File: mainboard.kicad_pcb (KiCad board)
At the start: 2 copper layers, 147 parts, among them IC1 ATXMEGA128A1U-A, J1 USB, K1 X_MIN, K2 X_MAX, K3 Y_MIN, K4 Y_MAX, K5 Z_MIN, K6 Z_MAX, P1 POWER, P10 USART, P11 TH_HB, P12 TH_EX, P13 TH_HO, P14 LCD, P15 STP_Y, P16 STP_E0, P17 STP_X, P18 STP_E1, P19 STP_Z, P2 PDI, P20 EXTR, P21 HIC_0, P22 HEATBED, P23 HIC_1, P24 FAN_0, P25 FAN_1, P26 LOC_0, P27 LOC_1, P3 GPIO_B, P4 BEEPER, P5 OPEN_C_OUT, P6 12V, P7 5V, P8 3.3V, P9 I2C, Q1 IRL1404, Q2 IRL1404, Q3 IRL1404, Q4 IRL1404, U1 NE 4558 D SMD, U10 ULN_2003_A, U2 ULN_2003_A, U3 A4988-BO, U4 A4988-BO, U5 A4988-BO, U6 A4988-BO, U7 A4988-BO, U8 MCP14E10, U9 MCP14E10

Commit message: Added missing interface connector; reworked schematic. Started to layout PCB
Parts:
- added D20: LOC0, LEDs:LED-0603, F.Cu at (157.7, 45.0)
- added D21: LOC1, LEDs:LED-0603, F.Cu at (184.2, 19.5)
- added R31: 4.7k, SMD_Packages:SM0805, F.Cu at (158.4, 42.0)
- added R32: 4.7k, SMD_Packages:SM0805, F.Cu at (162.3, 39.7)
- C1, C3: value 100n -> 470uF; footprint SMD_Packages:SM0603_Capa -> Capacitors_SMD:c_elec_10x10
- C17: value 100uF -> 100n; footprint Capacitors_SMD:c_elec_6.3x7.7 -> SMD_Packages:SM0603_Capa
- C2, C5: value 470uF -> 100n; footprint Capacitors_SMD:c_elec_10x10 -> SMD_Packages:SM0603_Capa
- C22: value 100n -> 100uF; footprint SMD_Packages:SM0603_Capa -> Capacitors_SMD:c_elec_6.3x7.7
- D10: value DIODE -> EXTR; footprint Diodes_SMD:Diode-SMA_Handsoldering -> LEDs:LED-0603
- D11: value DIODE -> HIC0; footprint Diodes_SMD:Diode-SMA_Handsoldering -> LEDs:LED-0603
- D12: value HIC1 -> DIODE; footprint LEDs:LED-0603 -> Diodes_SMD:Diode-MELF_Handsoldering
- D13: value HB -> DIODE; footprint LEDs:LED-0603 -> Diodes_SMD:Diode-MELF_Handsoldering
- D14: value DIODE -> HIC1; footprint Diodes_SMD:Diode-SMA_Handsoldering -> LEDs:LED-0603
- D15: value DIODE -> HB; footprint Diodes_SMD:Diode-SMA_Handsoldering -> LEDs:LED-0603
- D16: value FAN0 -> DIODE; footprint LEDs:LED-0603 -> Diodes_SMD:Diode-MELF_Handsoldering
- D17: value FAN1 -> DIODE; footprint LEDs:LED-0603 -> Diodes_SMD:Diode-MELF_Handsoldering
- D18: value LOC0 -> FAN0
- D19: value LOC1 -> FAN1
- D2: value PWR -> PRW 12V
- D3: value ST-E0 -> PWR 5V
- D4: value ST-Y -> PWR 3V3
- D5: value ST-E1 -> ST-E0
- D6: value ST-X -> ST-Y
- D7: value ST-Z -> ST-E1
- D8: value EXTR -> ST-X
- D9: value HIC0 -> ST-Z
- R10: value 5.6k -> 33k
- R12, R13: value 100k -> 5.6k
- R15, R16: value 15k -> 100k
- R18, R19: value 680 -> 15k
- R23, R24: value 4.7k -> 680
- R3: value 680 -> 4.7k
- R4: value 68 -> 1.5k
- R5: value 68 -> 680
- R6, R7: value 10k -> 68
- R8: value 33k -> 10k
- R9: value 5.6k -> 10k
- U10: footprint SMD_Packages:SO14E -> SMD_Packages:SO16E
- moved P3 333.0 mm to (336.5, -29.0)
- moved P14 311.7 mm to (337.5, 15.0)
- moved C12 311.2 mm to (326.0, 69.5)
- moved J1 305.9 mm to (329.5, 80.0)
- moved U2 287.2 mm to (338.0, 141.0)
- moved P5 286.0 mm to (336.5, 151.0)
- moved D1 270.8 mm to (278.5, 15.5)
- moved R6 264.6 mm to (332.5, 66.5)
- moved RV5 263.0 mm to (328.5, 26.0)
- moved C17 257.1 mm to (342.0, 24.5)
- moved R7 252.6 mm to (339.0, 69.0)
- moved VR2 229.9 mm to (327.0, 66.5)
- moved VR1 226.5 mm to (333.0, 69.0)
- moved R4 205.5 mm to (264.0, 36.5), turned to 90 degrees
- moved C8 191.9 mm to (214.5, 103.0), turned to 180 degrees
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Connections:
- C1 pad 1: GND -> +12V
- C1 pad 2: +3.3V -> GND
- C17 pad 1: +12V -> +5V
- C17 pad 2: Net-(C17-Pad2) -> GND
- C2 pad 1: +12V -> GND
- C2 pad 2: GND -> +3.3V
- C22 pad 1: +5V -> +12V
- C22 pad 2: GND -> Net-(C22-Pad2)
- C3 pad 1: GND -> +3.3V
- C3 pad 2: +3.3V -> GND
- C5 pad 1: +3.3V -> GND
- C5 pad 2: GND -> +3.3V
- C6 pad 1: GND -> +3.3V
- C6 pad 2: +3.3V -> GND
- C7 pad 1: +3.3V -> GND
- C7 pad 2: GND -> +3.3V
- D10 pad 2: +12V -> Net-(D10-Pad2)
- D11 pad 2: +12V -> Net-(D11-Pad2)
- D12 pad 1: Net-(D12-Pad1) -> Net-(D11-Pad2)
- D12 pad 2: Net-(D12-Pad2) -> +12V
- D13 pad 1: Net-(D13-Pad1) -> Net-(D10-Pad2)
- D13 pad 2: Net-(D13-Pad2) -> +12V
- D14 pad 1: Net-(D12-Pad2) -> Net-(D14-Pad1)
- D14 pad 2: +12V -> Net-(D14-Pad2)
- D15 pad 1: Net-(D13-Pad2) -> Net-(D15-Pad1)
- D15 pad 2: +12V -> Net-(D15-Pad2)
- D16 pad 1: Net-(D16-Pad1) -> Net-(D14-Pad2)
- D16 pad 2: Net-(D16-Pad2) -> +12V
- D17 pad 1: Net-(D17-Pad1) -> Net-(D15-Pad2)
- D17 pad 2: Net-(D17-Pad2) -> +12V
- D2 pad 1: +3.3V -> +12V
- D3 pad 1: Net-(D3-Pad1) -> +5V
- D4 pad 1: Net-(D4-Pad1) -> +3.3V
- D8 pad 2: Net-(D11-Pad1) -> Net-(D8-Pad2)
- D9 pad 2: Net-(D10-Pad1) -> Net-(D9-Pad2)
- P20 pad 2: Net-(D11-Pad1) -> Net-(D10-Pad2)
- P21 pad 2: Net-(D10-Pad1) -> Net-(D11-Pad2)
- P22 pad 2: Net-(D13-Pad2) -> Net-(D15-Pad2)
- P23 pad 2: Net-(D12-Pad2) -> Net-(D14-Pad2)
- P24 pad 2: Net-(D16-Pad2) -> Net-(D18-Pad2)
- P25 pad 2: Net-(D17-Pad2) -> Net-(D19-Pad2)
- P26 pad 2: Net-(D18-Pad2) -> Net-(D20-Pad2)
- P27 pad 2: Net-(D19-Pad2) -> Net-(D21-Pad2)
- Q1 pad D: Net-(D11-Pad1) -> Net-(D10-Pad2)
- Q2 pad D: Net-(D10-Pad1) -> Net-(D11-Pad2)
- Q3 pad D: Net-(D12-Pad2) -> Net-(D14-Pad2)
- Q4 pad D: Net-(D13-Pad2) -> Net-(D15-Pad2)
- R10 pad 1: GND -> Net-(R10-Pad1)
- R10 pad 2: Net-(P12-Pad2) -> GND
- R11 pad 2: Net-(P13-Pad2) -> Net-(P11-Pad2)
- R12 pad 1: Net-(P11-Pad2) -> GND
- R12 pad 2: /TH_HB -> Net-(P12-Pad2)
- R13 pad 1: Net-(P12-Pad2) -> GND
- R13 pad 2: /TH_EX -> Net-(P13-Pad2)
- R14 pad 1: Net-(P13-Pad2) -> Net-(P11-Pad2)
- R14 pad 2: /TH_HO -> /TH_HB
- R15 pad 1: +3.3V -> Net-(P12-Pad2)
- R15 pad 2: Net-(P11-Pad2) -> /TH_EX
- R16 pad 1: +3.3V -> Net-(P13-Pad2)
- R16 pad 2: Net-(P12-Pad2) -> /TH_HO
- R17 pad 2: Net-(P13-Pad2) -> Net-(P11-Pad2)
- R18 pad 1: Net-(D3-Pad2) -> +3.3V
- R18 pad 2: GND -> Net-(P12-Pad2)
- R19 pad 1: Net-(D4-Pad2) -> +3.3V
- R19 pad 2: GND -> Net-(P13-Pad2)
- R23 pad 1: +12V -> Net-(D8-Pad2)
- R23 pad 2: Net-(D8-Pad1) -> GND
- R24 pad 1: +12V -> Net-(D9-Pad2)
- R24 pad 2: Net-(D9-Pad1) -> GND
- R25 pad 2: Net-(D12-Pad1) -> Net-(D10-Pad1)
- R26 pad 2: Net-(D13-Pad1) -> Net-(D11-Pad1)
- R27 pad 1: Net-(D16-Pad1) -> +12V
- R27 pad 2: +12V -> Net-(D14-Pad1)
- R28 pad 1: Net-(D17-Pad1) -> +12V
- R28 pad 2: +12V -> Net-(D15-Pad1)
- R4 pad 1: Net-(IC1-Pad31) -> Net-(D3-Pad2)
- R4 pad 2: Net-(J1-Pad2) -> GND
- R5 pad 1: Net-(IC1-Pad32) -> Net-(D4-Pad2)
- R5 pad 2: Net-(J1-Pad3) -> GND
- R6 pad 1: /TWIC-SDA -> Net-(IC1-Pad31)
- R6 pad 2: +3.3V -> Net-(J1-Pad2)
- R7 pad 1: /TWIC-SCL -> Net-(IC1-Pad32)
- R7 pad 2: +3.3V -> Net-(J1-Pad3)
- R8 pad 1: Net-(R8-Pad1) -> /TWIC-SDA
- R8 pad 2: GND -> +3.3V
- R9 pad 1: GND -> /TWIC-SCL
- R9 pad 2: Net-(P11-Pad2) -> +3.3V
- RV1 pad 2: Net-(R8-Pad1) -> Net-(R10-Pad1)
- U1 pad 2: Net-(R8-Pad1) -> Net-(R10-Pad1)
- U10 pad 10: Net-(D19-Pad2) -> Net-(D21-Pad2)
- U10 pad 12: Net-(D18-Pad2) -> Net-(D20-Pad2)
- U10 pad 14: Net-(D17-Pad2) -> Net-(D19-Pad2)
- U3 pad 15: Net-(C17-Pad2) -> Net-(C18-Pad2)
- U5 pad 15: Net-(C19-Pad2) -> Net-(C20-Pad2)
- U6 pad 15: Net-(C20-Pad2) -> Net-(C21-Pad2)
- U7 pad 15: Net-(C21-Pad2) -> Net-(C22-Pad2)

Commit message: Reworked schematic
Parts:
- moved JP1 5.90 mm to (80.0, 39.5)
- moved JP2 5.25 mm to (79.5, 44.5)
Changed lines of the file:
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@@
     (links 367)
     (no_connects 367)
-    (area 0 0 0 0)
+    (area 12.7 -35.71195 351.851001 196.031501)
     (thickness 1.6)
     (drawings 0)
@@
     (pad_to_mask_clearance 0)
     (aux_axis_origin 0 0)
-    (grid_origin 10 10)
+    (grid_origin 78 28)
     (visible_elements FFFFF77F)
     (pcbplotparams
@@
   )
   (module Connect:SIL-2 (layer F.Cu)
-    (at 79.491828 45.382018)
+    (at 80 39.5)
     (descr "Connecteurs 2 pins")
     (tags "CONN DEV")
@@
   )
   (module Connect:SIL-2 (layer F.Cu)
-    (at 79.491828 39.252018)
+    (at 79.5 44.5)
     (descr "Connecteurs 2 pins")
     (tags "CONN DEV")

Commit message: * Changed connectors to PSK type - this prevents plugging the steppers in the wrong way * Changed stepping increment jumpers to DIP-switches - easier setting
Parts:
- removed JP1, JP10, JP11, JP12, JP13, JP14, JP15, JP2, JP3, JP4, JP5, JP6, JP7, JP8, JP9: JUMPER, Connect:SIL-2
- added P28: INTERFACE, Connect:VASCH5x2, F.Cu at (243.0, 92.0)
- added SW1: Y, dip-s:DIPS-DS03, F.Cu at (0.00, 0.00)
- added SW2: E0, dip-s:DIPS-DS03, F.Cu at (0.00, 0.00)
- added SW3: X, dip-s:DIPS-DS03, F.Cu at (0.00, 0.00)
- added SW4: E1, dip-s:DIPS-DS03, F.Cu at (0.00, 0.00)
- added SW5: Z, dip-s:DIPS-DS03, F.Cu at (0.00, 0.00)
- P15, P16, P17, P18, P19: footprint Connect:bornier4 -> 3dp-special:PSS4
- P2, P9: footprint Connect:SIL-4 -> 3dp-special:PSS4
- P24, P25, P26, P27: footprint Connect:bornier2 -> Connect:SIL-2
- P5: value OPEN_C_OUT -> OPEN_COLL_D
- moved P16 176.3 mm to (50.0, 191.5)
- moved P18 123.7 mm to (4.00, 173.5)
- moved P15 109.2 mm to (74.5, 165.5)
- moved P17 102.2 mm to (51.0, 139.0)
- moved P19 78.4 mm to (24.0, 135.0)
- moved D12 9.90 mm to (152.0, 34.5)
- moved D18 9.62 mm to (175.0, 41.9)
- moved D19 9.62 mm to (171.1, 44.2)
- moved R26 9.62 mm to (167.9, 41.2)
- moved R31 9.62 mm to (167.9, 43.5)
- moved R32 9.62 mm to (171.8, 41.2)
- moved C22 7.44 mm to (50.5, 48.5)
- moved D16 2.15 mm to (153.0, 39.0)
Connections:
- net /A0 renamed /OCD_1
- net /A1 renamed /OCD_2
- net /A2 renamed /OCD_3
- net /A3 renamed /OCD_4
- net /A4 renamed /OCD_5
- net /A5 renamed /OCD_6
- net /B0 renamed /GPIOB_0
- net /B1 renamed /GPIOB_1
- net /B2 renamed /GPIOB_2
- net /B3 renamed /GPIOB_3
- net /B4 renamed /GPIOB_4
- net /B5 renamed /GPIOB_5
- net /B6 renamed /GPIOB_6
- net /B7 renamed /GPIOB_7
- net Net-(J1-Pad2) renamed /USB-
- net Net-(J1-Pad3) renamed /USB+
- IC1 pad 1: /INP_INTERF4 -> /INTERF4
- IC1 pad 100: /INP_INTERF3 -> /INTERF3
- IC1 pad 2: /INP_INTERF5 -> /INTERF5
- IC1 pad 98: /INP_INTERF1 -> /INTERF1
- IC1 pad 99: /INP_INTERF2 -> /INTERF2
- U4 pad 15: Net-(U4-Pad15) -> Net-(C19-Pad2)
- U4 pad 16: Net-(U4-Pad16) -> +12V

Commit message: * Added PSK-2 connector to library * Changed Low-Current outputs (FANs etc) to PSK-2 connectors
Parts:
- K1, K2, K3, K4, K5, K6: footprint Connect:PINHEAD1-3 -> 3dp-special:PSS3
- P24, P25, P26, P27: footprint Connect:SIL-2 -> 3dp-special:PSS2
- moved SW1 216.6 mm to (120.5, 180.0)
- moved SW2 208.2 mm to (41.5, 204.0)
- moved P8 200.9 mm to (240.5, 37.0)
- moved SW3 190.7 mm to (101.5, 161.5)
- moved SW4 185.8 mm to (26.0, 184.0)
- moved SW5 167.8 mm to (40.0, 163.0)
- moved P24 150.8 mm to (187.0, 156.0)
- moved P26 145.6 mm to (197.5, 150.5)
- moved P27 143.8 mm to (206.0, 151.5)
- moved D21 140.6 mm to (223.5, 154.5)
- moved U10 140.1 mm to (198.5, 161.0)
- moved P2 129.1 mm to (189.5, 73.0)
- moved D20 127.8 mm to (214.5, 159.5)
- moved R26 127.4 mm to (233.9, 150.2)
- moved R32 127.4 mm to (237.8, 150.2)
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
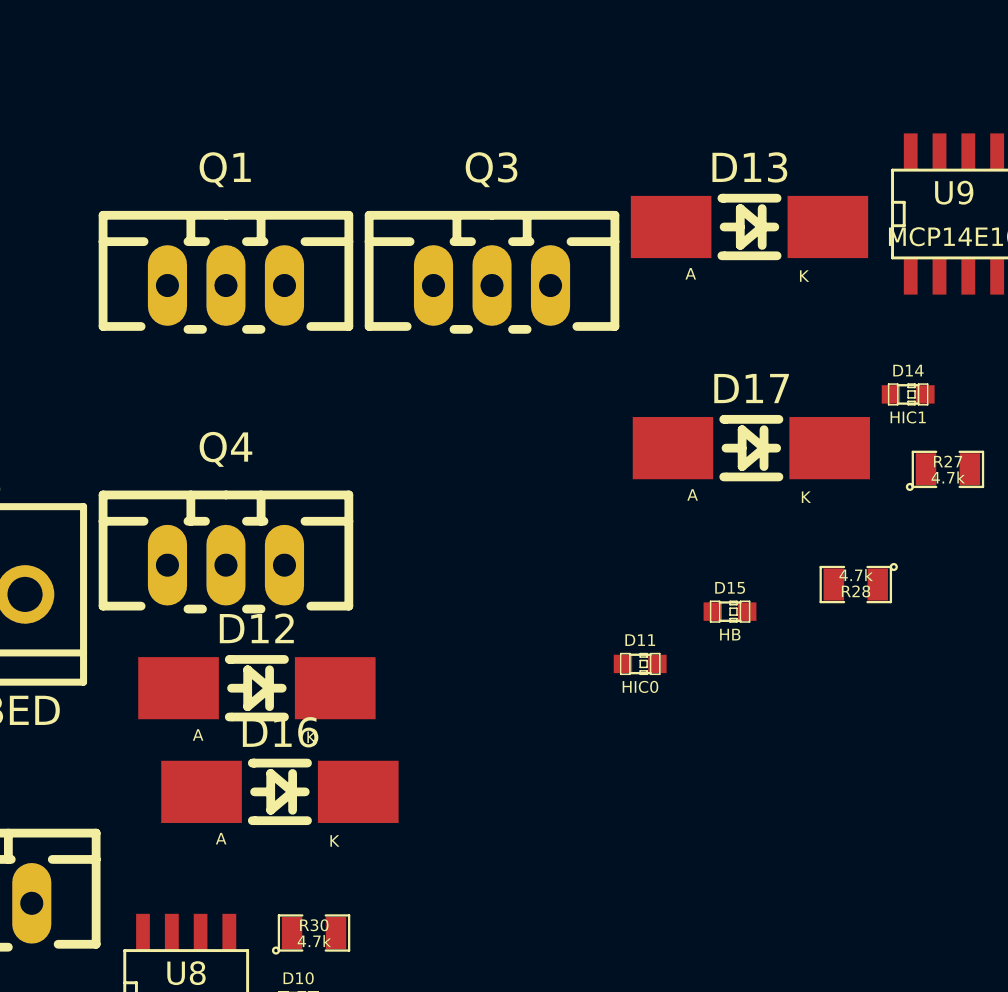
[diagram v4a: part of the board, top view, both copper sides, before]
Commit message: Added footprint for SOD323 diode package and replaced former MELF-package
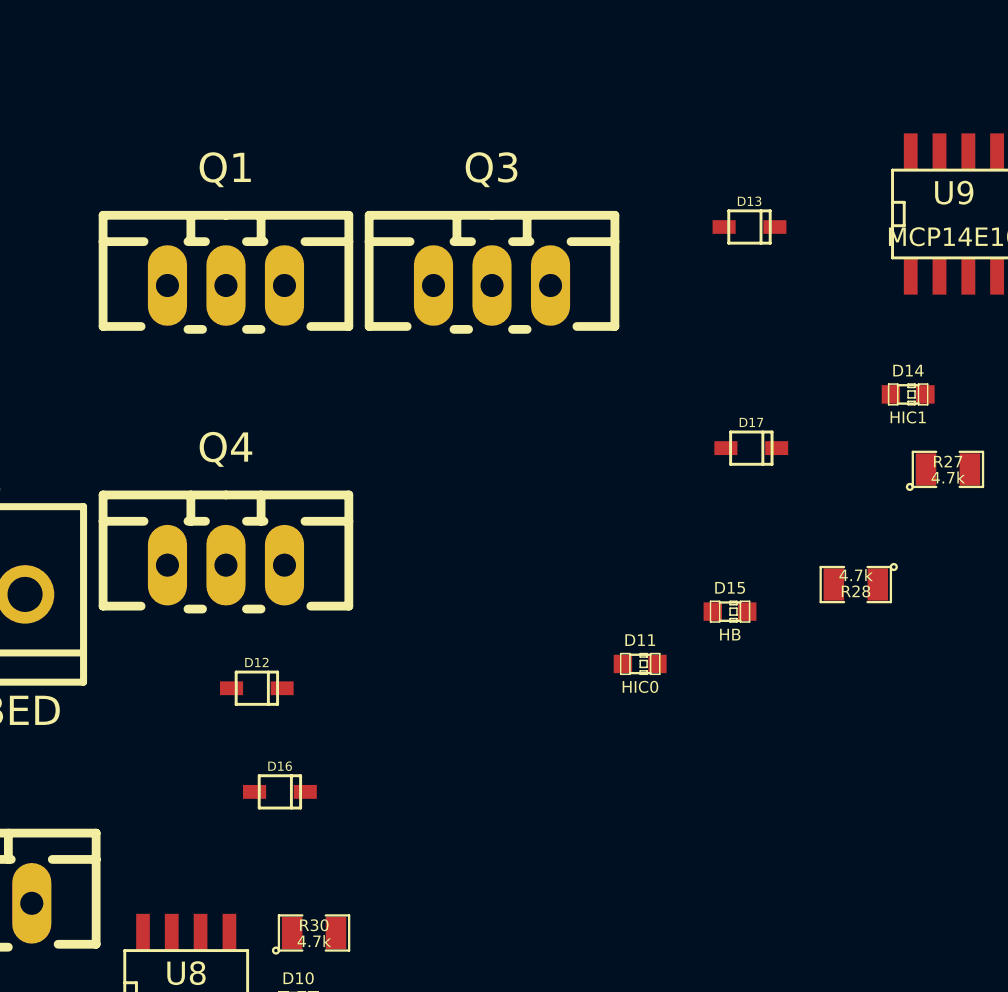
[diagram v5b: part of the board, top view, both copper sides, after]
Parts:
- D12, D13, D16, D17: footprint Diodes_SMD:Diode-MELF_Handsoldering -> smd-diode:SOD323

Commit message: Changed USART connector to show the respective net each pin is connected to
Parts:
- moved C3 204.2 mm to (253.0, 24.0)
- moved C19 195.2 mm to (32.5, 206.5)
- moved C1 181.1 mm to (268.5, 23.5)
- moved C18 173.6 mm to (103.5, 188.5)
- moved C21 154.9 mm to (41.0, 180.0)
- moved P3 140.6 mm to (243.5, 76.5)
- moved VR4 132.4 mm to (218.5, 98.0)
- moved R21 119.9 mm to (21.7, 154.0)
- moved R22 119.9 mm to (17.8, 154.0)
- moved R23 119.9 mm to (13.9, 154.0)
- moved R24 119.9 mm to (10.0, 154.0)
- moved C20 118.9 mm to (98.5, 149.0)
- moved R20 115.3 mm to (16.0, 157.5)
- moved VR6 103.8 mm to (204.0, 97.0)
- moved VR3 103.8 mm to (207.2, 99.3)
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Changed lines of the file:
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@@
     (links 376)
     (no_connects 376)
-    (area 0 0 0 0)
+    (area 7.92 8.28805 351.851001 211.306401)
     (thickness 1.6)
     (drawings 0)
@@
     (add_net Z_STEP)
   )
+  (module Connect:SIL-5 (layer F.Cu)
+    (at 35.926401 103.382018)
+    (descr "Connecteur 5 pins")
+    (tags "CONN DEV")
+    (fp_text reference P10 (at 3.635 -2.14) (layer F.SilkS)
+      (effects (font (size 1.02974 1.08712) (thickness 0.257435)))
+    )
+    (fp_text value USART (at -5.28 -2.14) (layer F.SilkS)
+      (effects (font (size 1.024 1.016) (thickness 0.254)))
+    )
+    (fp_text user 3V3 (at 3.81 2.54 90) (layer F.SilkS)
+      (effects (font (size 0.8 0.8) (thickness 0.15)))
+    )
+    (fp_text user XCK (at 1.27 2.54 90) (layer F.SilkS)
+      (effects (font (size 0.8 0.8) (thickness 0.15)))
+    )
+    (fp_text user RX (at -1.27 2.54 90) (layer F.SilkS)
+      (effects (font (size 0.8 0.8) (thickness 0.15)))
+    )
+    (fp_text user TX (at -3.81 2.54 90) (layer F.SilkS)
+      (effects (font (size 0.8 0.8) (thickness 0.15)))
+    )
+    (fp_text user GND (at -6.35 2.54 90) (layer F.SilkS)
+      (effects (font (size 0.8 0.8) (thickness 0.15)))
+    )
+    (fp_line (start -7.62 1.27) (end -7.62 -1.27) (layer F.SilkS) (width 0.3048))
+    (fp_line (start -7.62 -1.27) (end 5.08 -1.27) (layer F.SilkS) (width 0.3048))
+    (fp_line (start 5.08 -1.27) (end 5.08 1.27) (layer F.SilkS) (width 0.3048))
+    (fp_line (start 5.08 1.27) (end -7.62 1.27) (layer F.SilkS) (width 0.3048))
+    (fp_line (start -5.08 1.27) (end -5.08 -1.27) (layer F.SilkS) (width 0.3048))
+    (pad 1 thru_hole rect (at -6.35 0) (size 1.397 1.397) (drill 0.8128) (layers *.Cu *.Mask F.SilkS)
+      (net 2 GND))
+    (pad 2 thru_hole circle (at -3.81 0) (size 1.397 1.397) (drill 0.8128) (layers *.Cu *.Mask F.SilkS)
+      (net 88 /USARTC1-TXD1))
+    (pad 3 thru_hole circle (at -1.27 0) (size 1.397 1.397) (drill 0.8128) (layers *.Cu *.Mask F.SilkS)
+      (net 87 /USARTC1-RXD1))
+    (pad 4 thru_hole circle (at 1.27 0) (size 1.397 1.397) (drill 0.8128) (layers *.Cu *.Mask F.SilkS)
+      (net 86 /USARTC1-XCK1))
+    (pad 5 thru_hole circle (at 3.81 0) (size 1.397 1.397) (drill 0.8128) (layers *.Cu *.Mask F.SilkS)
+      (net 3 +3.3V))
+  )
   (module SMD_Packages:SM0603_Capa (layer F.Cu)
     (at 225.5 123)
@@
   )
   (module Capacitors_SMD:c_elec_6.3x7.7 (layer F.Cu)
-    (at 102.05441 14.880336)
+    (at 103.5 188.5)
     (descr "SMT capacitor, aluminium electrolytic, 6.3x7.7")
     (fp_text reference C18 (at 0 -3.937) (layer F.SilkS)
@@
   )
   (module Capacitors_SMD:c_elec_6.3x7.7 (layer F.Cu)
-    (at 102.05441 24.070336)
+    (at 32.5 206.5)
     (descr "SMT capacitor, aluminium electrolytic, 6.3x7.7")
     (fp_text reference C19 (at 0 -3.937) (layer F.SilkS)
@@
   )
   (module Capacitors_SMD:c_elec_6.3x7.7 (layer F.Cu)
-    (at 90.52441 30.320336)
+    (at 98.5 149)
     (descr "SMT capacitor, aluminium electrolytic, 6.3x7.7")
     (fp_text reference C20 (at 0 -3.937) (layer F.SilkS)
@@
   )
   (module Capacitors_SMD:c_elec_6.3x7.7 (layer F.Cu)
-    (at 80.92441 30.320336)
+    (at 41 180)
     (descr "SMT capacitor, aluminium electrolytic, 6.3x7.7")
     (fp_text reference C21 (at 0 -3.937) (layer F.SilkS)
@@
   )
   (module Connect:VASCH5x2 (layer F.Cu)
-    (at 336.5 -29)
+    (at 243.5 76.5)
     (descr CONNECTOR)
     (tags CONNECTOR)
@@
       (net 3 +3.3V))
   )
-  (module Connect:SIL-5 (layer F.Cu)
-    (at 35.926401 103.382018)
-    (descr "Connecteur 5 pins")
-    (tags "CONN DEV")
-    (fp_text reference P10 (at -0.635 -2.54) (layer F.SilkS)
-      (effects (font (size 1.72974 1.08712) (thickness 0.3048)))
-    )
-    (fp_text value USART (at 0 -2.54) (layer F.SilkS) hide
-      (effects (font (size 1.524 1.016) (thickness 0.3048)))
-    )
-    (fp_line (start -7.62 1.27) (end -7.62 -1.27) (layer F.SilkS) (width 0.3048))
-    (fp_line (start -7.62 -1.27) (end 5.08 -1.27) (layer F.SilkS) (width 0.3048))
-    (fp_line (start 5.08 -1.27) (end 5.08 1.27) (layer F.SilkS) (width 0.3048))
-    (fp_line (start 5.08 1.27) (end -7.62 1.27) (layer F.SilkS) (width 0.3048))
-    (fp_line (start -5.08 1.27) (end -5.08 -1.27) (layer F.SilkS) (width 0.3048))
-    (pad 1 thru_hole rect (at -6.35 0) (size 1.397 1.397) (drill 0.8128) (layers *.Cu *.Mask F.SilkS)
-      (net 2 GND))
-    (pad 2 thru_hole circle (at -3.81 0) (size 1.397 1.397) (drill 0.8128) (layers *.Cu *.Mask F.SilkS)
-      (net 88 /USARTC1-TXD1))
-    (pad 3 thru_hole circle (at -1.27 0) (size 1.397 1.397) (drill 0.8128) (layers *.Cu *.Mask F.SilkS)
-      (net 87 /USARTC1-RXD1))
-    (pad 4 thru_hole circle (at 1.27 0) (size 1.397 1.397) (drill 0.8128) (layers *.Cu *.Mask F.SilkS)
-      (net 86 /USARTC1-XCK1))
-    (pad 5 thru_hole circle (at 3.81 0) (size 1.397 1.397) (drill 0.8128) (layers *.Cu *.Mask F.SilkS)
-      (net 3 +3.3V))
-  )
   (module Connect:PINHEAD1-2 (layer F.Cu)
     (at 87.141001 87.534)
@@
   )
   (module SMD_Packages:SM0805 (layer F.Cu)
-    (at 78.171531 60.395596)
+    (at 16 157.5)
     (attr smd)
     (fp_text reference R20 (at 0 -0.3175) (layer F.SilkS)
@@
   )
   (module SMD_Packages:SM0805 (layer F.Cu)
-    (at 72.701531 45.475596)
+    (at 21.701531 153.975596)
     (attr smd)
     (fp_text reference R21 (at 0 -0.3175) (layer F.SilkS)
@@
   )
   (module SMD_Packages:SM0805 (layer F.Cu)
-    (at 68.801531 45.475596)
+    (at 17.801531 153.975596)
     (attr smd)
     (fp_text reference R22 (at 0 -0.3175) (layer F.SilkS)
@@
   )
   (module SMD_Packages:SM0805 (layer F.Cu)
-    (at 64.901531 45.475596)
+    (at 13.901531 153.975596)
     (attr smd)
     (fp_text reference R23 (at 0 -0.3175) (layer F.SilkS)
@@
   )
   (module SMD_Packages:SM0805 (layer F.Cu)
-    (at 61.001531 45.475596)
+    (at 10.001531 153.975596)
     (attr smd)
     (fp_text reference R24 (at 0 -0.3175) (layer F.SilkS)
@@
   )
   (module SMD_Packages:SM0805 (layer F.Cu)
-    (at 103.651531 91.805596)
+    (at 207.151531 99.305596)
     (attr smd)
     (fp_text reference VR3 (at 0 -0.3175) (layer F.SilkS)
@@
   )
   (module SMD_Packages:SM0805 (layer F.Cu)
-    (at 86.891531 112.235596)
+    (at 218.5 98)
     (attr smd)
     (fp_text reference VR4 (at 0 -0.3175) (layer F.SilkS)
@@
   )
   (module SMD_Packages:SM0805 (layer F.Cu)
-    (at 104.421531 89.535596)
+    (at 207.921531 97.035596)
     (attr smd)
     (fp_text reference VR5 (at 0 -0.3175) (layer F.SilkS)
@@
   )
   (module SMD_Packages:SM0805 (layer F.Cu)
-    (at 100.521531 89.535596)
+    (at 204.021531 97.035596)
     (attr smd)
     (fp_text reference VR6 (at 0 -0.3175) (layer F.SilkS)
@@
   )
   (module SMD_Packages:SM0805 (layer F.Cu)
-    (at 104.421531 87.265596)
+    (at 207.921531 94.765596)
     (attr smd)
     (fp_text reference VR7 (at 0 -0.3175) (layer F.SilkS)
@@
   )
   (module Capacitors_SMD:c_elec_10x10 (layer F.Cu)
-    (at 118.5 125)
+    (at 268.5 23.5)
     (descr "SMT capacitor, aluminium electrolytic, 10x10")
     (fp_text reference C1 (at 0 -5.842) (layer F.SilkS)
@@
   )
   (module Capacitors_SMD:c_elec_10x10 (layer F.Cu)
-    (at 62.05205 96.407065)
+    (at 253 24)
     (descr "SMT capacitor, aluminium electrolytic, 10x10")
     (fp_text reference C3 (at 0 -5.842) (layer F.SilkS)
@@
   )
   (module Capacitors_SMD:c_elec_6.3x7.7 (layer F.Cu)
-    (at 50.5 48.5)
+    (at 45 149.5)
     (descr "SMT capacitor, aluminium electrolytic, 6.3x7.7")
     (fp_text reference C22 (at 0 -3.937) (layer F.SilkS)
@@
   )
   (module 3dp-special:PSS4 (layer F.Cu)
-    (at 79.5 205)
+    (at 13 208)
     (descr "Connecteur 4 pibs")
     (tags CONN)
@@
   )
   (module 3dp-special:PSS4 (layer F.Cu)
-    (at 195.5 60.5)
+    (at 204.5 73)
     (descr "Connecteur 4 pibs")
     (tags CONN)
